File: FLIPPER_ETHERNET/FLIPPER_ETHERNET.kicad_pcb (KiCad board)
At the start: 2 copper layers, 31 parts, among them IC1 MC74ACT125DTR2G, J1 RJ45_Hanrun_HR911105A_Horizon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, J2 Screw_Terminal_01x06, SW1 SW_Push, T1 HX1188NLT, U1 ENC28J60x-ML, Y1 25MHz

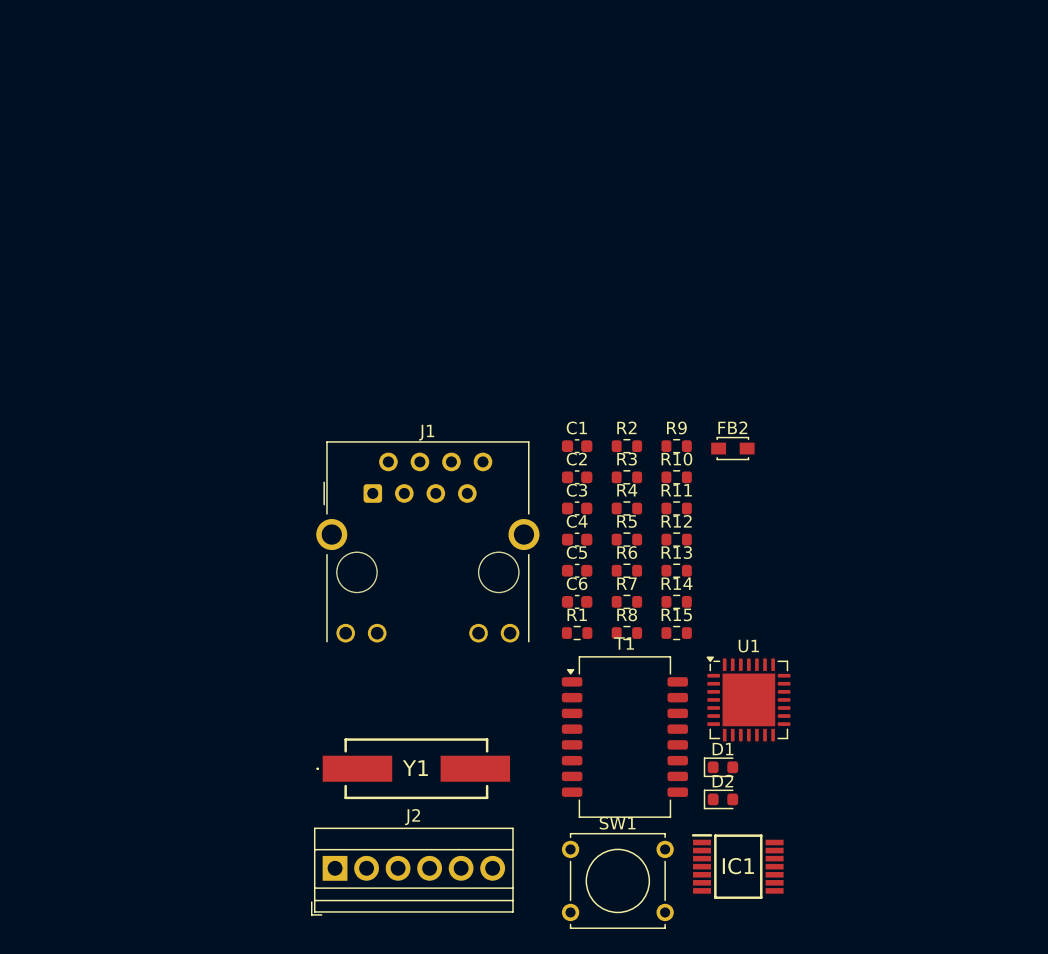
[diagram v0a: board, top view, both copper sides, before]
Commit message: feat: component reduction in the schematic of flipper ethernet and pcb first draft
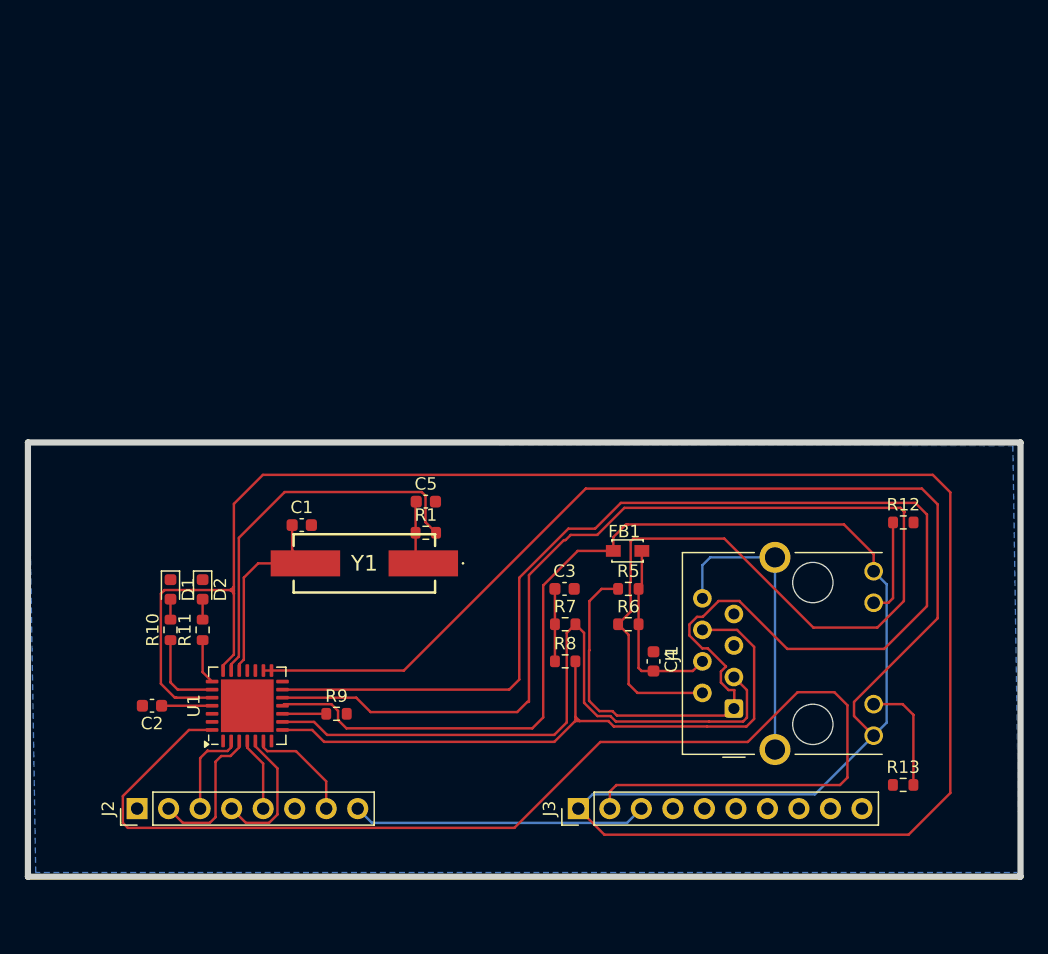
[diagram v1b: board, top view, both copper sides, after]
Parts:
- removed C6: 18pF, Capacitor_SMD:C_0603_1608Metric
- removed FB2: ILBB0805ER202V, Inductor_SMD:L_Walsin_WLFM201209x
- removed IC1: MC74ACT125DTR2G, FLIPPER_ETHERNET:MC74ACT125DTR2G
- removed R14: 100R, Resistor_SMD:R_0603_1608Metric
- removed R15: 10K, Resistor_SMD:R_0603_1608Metric
- removed R2, R3, R4: 75R, Resistor_SMD:R_0603_1608Metric
- removed SW1: SW_Push, Button_Switch_THT:SW_Tactile_Straight_KSA0Axx1LFTR
- removed T1: HX1188NLT, Transformer_SMD:Transformer_Pulse_H1100NL
- added FB1: FerriteBead, Inductor_SMD:L_Walsin_WLFM201209x, F.Cu at (159.3, 87.4)
- added J3: Conn_01x10_Socket, Connector_PinHeader_2.54mm:PinHeader_1x10_P2.54mm_Vertical, F.Cu at (155.3, 108.2)
- C1: value 1nF -> 18pF
- J2: value Screw_Terminal_01x06 -> Conn_01x08_Socket; footprint TerminalBlock:TerminalBlock_Xinya_XY308-2.54-6P_1x06_P2.54mm_Horizontal -> Connector_PinHeader_2.54mm:PinHeader_1x08_P2.54mm_Vertical
- R1: value 75R -> 100R
- moved D1 46.8 mm to (122.5, 90.5), turned to -90 degrees
- moved D2 45.2 mm to (125.0, 90.5), turned to -90 degrees
- moved R10 42.6 mm to (122.5, 93.8), turned to 90 degrees
- moved U1 40.4 mm to (128.6, 99.9), turned to 90 degrees
- moved R11 39.4 mm to (125.0, 93.8), turned to 90 degrees
- moved C2 38.9 mm to (121.0, 99.9), turned to 180 degrees
- moved R9 34.9 mm to (135.8, 100.5)
- moved J1 33.9 mm to (167.9, 100.1), turned to 90 degrees
- moved R13 25.1 mm to (181.5, 106.2), turned to 180 degrees
- moved C1 23.1 mm to (133.0, 85.3)
- moved R12 18.3 mm to (181.5, 85.1)
- moved Y1 17.1 mm to (138.1, 88.4), turned to 180 degrees
- moved J2 16.7 mm to (119.8, 108.2), turned to 90 degrees
- moved R1 14.6 mm to (143.0, 85.9)
- moved C5 13.4 mm to (143.0, 83.4)
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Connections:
- net Net-(U1-LEDA) renamed /LEDA
- net Net-(U1-LEDB) renamed /LEDB
- C1 pad 1: Net-(C1-Pad1) -> /OSC1
- C5 pad 1: /OSC1 -> Net-(C5-Pad1)
- J1 pad 1: /TX+ -> /TD+
- J1 pad 2: /TX- -> /TD-
- J1 pad 3: /RX+ -> /RD+
- J1 pad 4: Net-(J1-RCT) -> /TCT
- J1 pad 5: Net-(J1-RCT) -> unconnected-(J1-RCT-Pad5)
- J1 pad 6: /RX- -> /RD-
- J1 pad 8: Net-(J1-Pad8) -> GND
- J2 pad 1: /CS -> unconnected-(J2-Pin_1-Pad1)
- J2 pad 2: /MSCK -> /SI
- J2 pad 3: /MSO -> /SO
- J2 pad 4: /MSI -> /CS
- J2 pad 5: /MOSC1 -> /SCK
- J2 pad 6: /MINT0 -> unconnected-(J2-Pin_6-Pad6)
- R1 pad 1: /CMT_R -> Net-(C5-Pad1)
- R1 pad 2: Net-(C1-Pad1) -> /OSC2
- R5 pad 1: /TPOUT+ -> /TD+
- R6 pad 2: /TPOUT- -> /TD-
- R7 pad 1: /TPIN+ -> /RD+
- R8 pad 2: /TPIN- -> /RD-
- U1 pad 12: /TPOUT- -> /TD-
- U1 pad 13: /TPOUT+ -> /TD+
- U1 pad 27: /CLKOUT -> unconnected-(U1-CLKOUT-Pad27)
- U1 pad 3: /MSO -> /SI
- U1 pad 4: /MSCK -> /SCK
- U1 pad 6: /RESET -> /RST
- U1 pad 8: /TPIN- -> /RD-
- U1 pad 9: /TPIN+ -> /RD+
- Y1 pad 1: Net-(C6-Pad1) -> Net-(C5-Pad1)
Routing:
- net +3.3V: track 0.00 -> 336.7 mm
- net /TD+: track 0.00 -> 126.0 mm
- net /TD-: track 0.00 -> 115.4 mm
- net /INT: track 0.00 -> 101.9 mm
- net /RD+: track 0.00 -> 56.2 mm
- net /RD-: track 0.00 -> 55.4 mm
- net GND: track 0.00 -> 48.1 mm
- net /OSC2: track 0.00 -> 31.0 mm
- net /OSC1: track 0.00 -> 17.3 mm
- net /TCT: track 0.00 -> 15.1 mm
- net /SI: track 0.00 -> 11.8 mm
- net /CS: track 0.00 -> 11.1 mm
- net Net-(J1-Pad10): track 0.00 -> 9.21 mm
- net /RST: track 0.00 -> 8.91 mm
- net Net-(J1-Pad11): track 0.00 -> 7.82 mm
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- added copper zone on B.Cu, net (none)
- added copper zone on F.Cu, net GND
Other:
- board outline added: 80 x 35 mm

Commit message: feat: second draft of flipper ethernet pcb
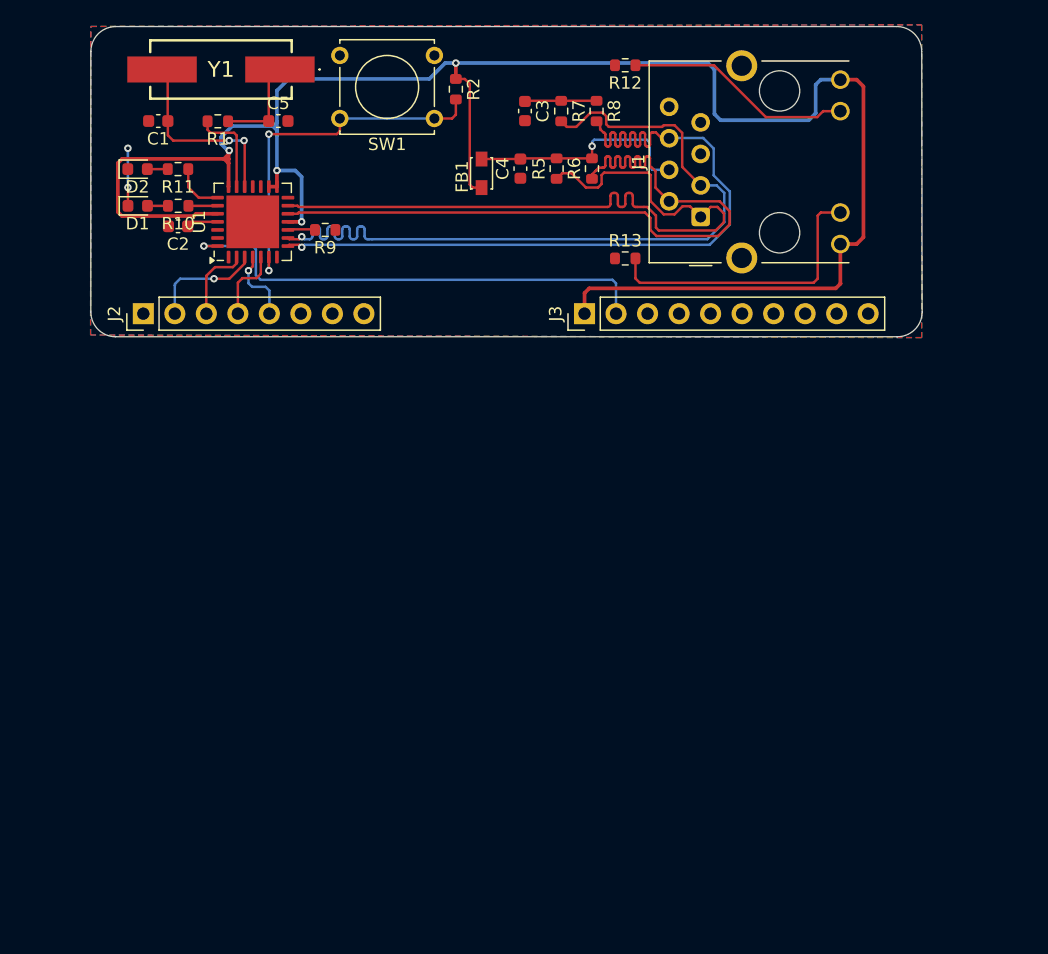
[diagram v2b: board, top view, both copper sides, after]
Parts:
- added R2: 10K, Resistor_SMD:R_0603_1608Metric, F.Cu at (145.4, 50.2)
- added SW1: SW_Push, Button_Switch_THT:SW_Tactile_Straight_KSA0Axx1LFTR, F.Cu at (143.7, 52.5)
- moved R13 48.0 mm to (159.1, 63.8)
- moved R8 44.4 mm to (156.8, 51.9), turned to -90 degrees
- moved R12 43.1 mm to (159.1, 48.2), turned to 180 degrees
- moved Y1 41.4 mm to (126.5, 48.6)
- moved R7 41.4 mm to (153.9, 51.9), turned to 90 degrees
- moved C4 41.1 mm to (150.7, 56.6), turned to -90 degrees
- moved J2 39.9 mm to (120.3, 68.3)
- moved J3 39.9 mm to (155.8, 68.3)
- moved J1 39.7 mm to (165.2, 60.5)
- moved R9 39.0 mm to (134.9, 61.5)
- moved U1 39.0 mm to (129.1, 60.9)
- moved C2 38.7 mm to (123.1, 61.2)
- moved C3 38.6 mm to (151.0, 51.9), turned to -90 degrees
- moved R11 37.2 mm to (123.1, 56.6), turned to 180 degrees
- moved R1 37.2 mm to (126.3, 52.8), turned to 180 degrees
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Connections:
- J2 pad 7: /RST -> unconnected-(J2-Pin_7-Pad7)
- U1 pad 6: /RST -> /RESET
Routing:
- net +3.3V: track 336.7 -> 154.8 mm, vias 0 -> 4
- net /TD+: track 126.0 -> 60.0 mm
- net /INT: track 101.9 -> 39.2 mm, vias 0 -> 1
- net /TD-: track 115.4 -> 60.0 mm
- net GND: track 48.1 -> 4.64 mm, vias 0 -> 2
- net /RESET: track 0.00 -> 29.6 mm, vias 0 -> 2
- net /OSC2: track 31.0 -> 7.34 mm
- net Net-(J1-Pad10): track 9.21 -> 23.6 mm
- net Net-(J1-Pad11): track 7.82 -> 18.5 mm
- net /RST: track 8.91 -> 0.00 mm
- net /RD-: track 55.4 -> 63.5 mm, vias 0 -> 1
- net /RD+: track 56.2 -> 63.4 mm, vias 0 -> 1
- net /CS: track 11.1 -> 6.00 mm
- net /LEDA: track 7.00 -> 2.35 mm
- net /TCT: track 15.1 -> 18.7 mm, vias 0 -> 1
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- added copper zone on B.Cu, net GND
- removed copper zone on B.Cu, net (none)
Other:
- board size 80 x 35 mm -> 67 x 25 mm

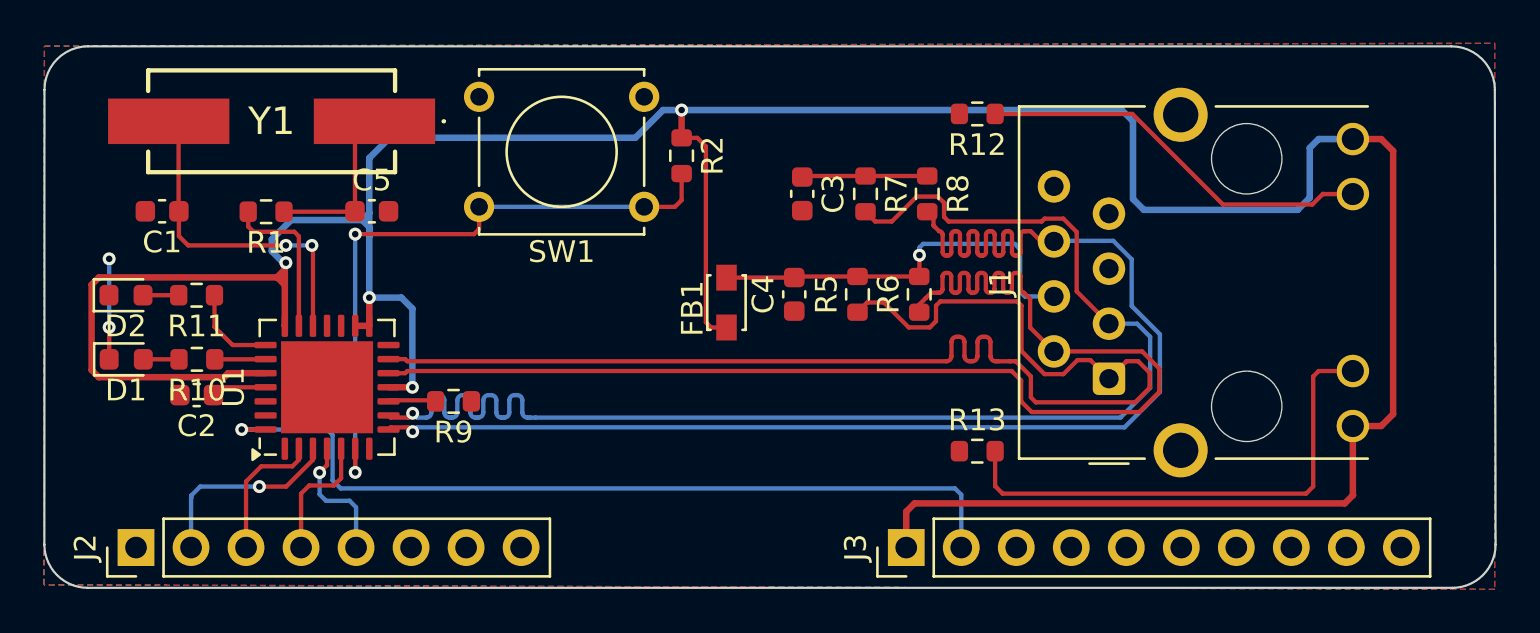
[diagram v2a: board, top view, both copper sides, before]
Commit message: feat: pcb corrected for possible first flipper ethernet prototype
all 3d models added
all labels added and reorganized
button changed for smd metal button
components reorganized
leds deleted
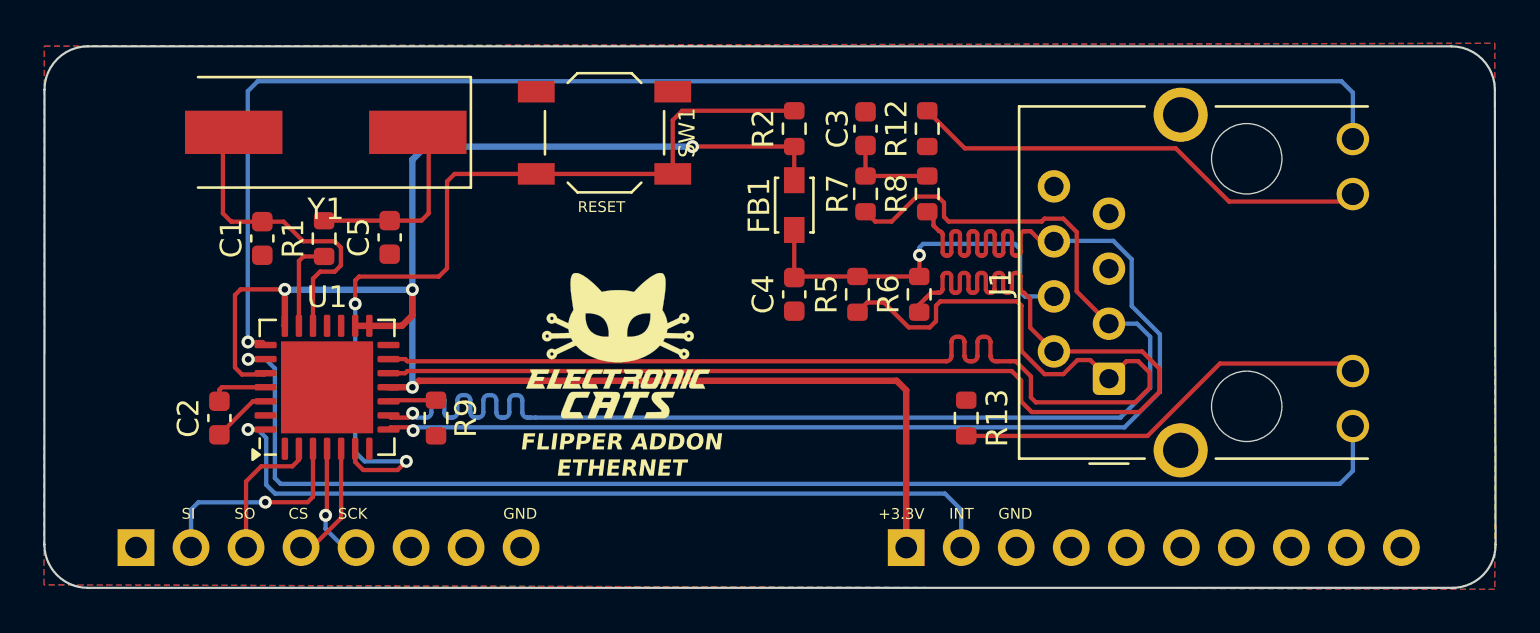
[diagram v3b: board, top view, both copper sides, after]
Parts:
- removed D1, D2: LED, LED_SMD:LED_0603_1608Metric
- removed R10, R11: 30R, Resistor_SMD:R_0603_1608Metric
- added G***: LOGO, Aesthetics:electronic_cats_logo_8x6, F.Cu at (142.5, 59.0)
- added G***: LOGO, Aesthetics:electronic_cats_logo_8x6, B.Cu at (142.5, 59.0)
- added REF**: OSHW-Logo2_9.8x8mm_SilkScreen, Symbol:OSHW-Logo2_9.8x8mm_SilkScreen, B.Cu at (153.7, 60.4)
- J2, J3: moved to B.Cu
- SW1: footprint Button_Switch_THT:SW_Tactile_Straight_KSA0Axx1LFTR -> Button_Switch_SMD:SW_SPST_TL3342
- Y1: footprint FLIPPER_ETHERNET:ABLS-25.000MHZ-20-F-T -> Crystal:Crystal_SMD_HC49-SD
- moved FB1 5.48 mm to (150.7, 52.5), turned to -90 degrees
- moved R2 5.35 mm to (150.7, 48.9), turned to 90 degrees
- moved C1 4.79 mm to (126.1, 54.0), turned to -90 degrees
- moved C3 4.19 mm to (153.9, 48.9), turned to 90 degrees
- moved SW1 3.88 mm to (141.9, 49.1)
- moved R1 2.95 mm to (128.9, 54.0), turned to -90 degrees
- moved Y1 2.55 mm to (129.0, 49.1)
- moved R12 2.41 mm to (156.8, 48.9), turned to -90 degrees
- moved R13 1.61 mm to (158.6, 62.3), turned to 90 degrees
- moved C2 1.49 mm to (124.1, 62.3), turned to -90 degrees
- moved C5 1.46 mm to (132.0, 54.0), turned to -90 degrees
- moved R9 1.12 mm to (134.1, 62.3), turned to -90 degrees
- turned J2 to -90 degrees
- turned J3 to -90 degrees
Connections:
- J1 pad 12: +3.3V -> /LEDB
- J1 pad 9: +3.3V -> /LEDA
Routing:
- net +3.3V: track 154.8 -> 80.4 mm
- net /LEDB: track 4.17 -> 66.0 mm, vias 0 -> 1
- net /LEDA: track 2.35 -> 59.5 mm, vias 0 -> 1
- net /RESET: track 29.6 -> 41.1 mm
- net Net-(J1-Pad10): track 23.6 -> 19.4 mm
- net /OSC2: track 7.34 -> 4.24 mm
- net Net-(J1-Pad11): track 18.5 -> 21.5 mm
- net GND: track 4.64 -> 2.77 mm, vias 2 -> 0
- net Net-(D2-A): track 1.65 -> 0.00 mm
- net Net-(D1-A): track 1.65 -> 0.00 mm
- net Net-(C3-Pad1): track 5.80 -> 4.27 mm
- net /INT: track 39.2 -> 38.3 mm
- net /TCT: track 18.7 -> 17.8 mm
- net Net-(C5-Pad1): track 7.82 -> 8.71 mm
- net /OSC1: track 15.9 -> 15.0 mm, vias 2 -> 0
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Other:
- board text added: "+3.3V"
- board text added: "CS"
- board text added: "FLIPPER ADDON ETHERNET"
- board text added: "GND"
- board text added: "INT"
- board text added: "RESET"
- board text added: "SCK"
- board text added: "SI"
- board text added: "SO"

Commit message: feat: add labels
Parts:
- added kibuzzard-6706978D: G***, kibuzzard-6706978D, F.Cu at (142.0, 53.4)
- added kibuzzard-670697AB: G***, kibuzzard-670697AB, F.Cu at (130.8, 66.0)
- added kibuzzard-670697C4: G***, kibuzzard-670697C4, F.Cu at (127.7, 65.8)
- added kibuzzard-670697CE: G***, kibuzzard-670697CE, F.Cu at (125.2, 65.7)
- added kibuzzard-670697DC: G***, kibuzzard-670697DC, F.Cu at (122.8, 65.9)
- added kibuzzard-6706980D: G***, kibuzzard-6706980D, F.Cu at (137.7, 66.0)
- added kibuzzard-6706982B: G***, kibuzzard-6706982B, F.Cu at (161.4, 66.2)
- added kibuzzard-67069833: G***, kibuzzard-67069833, F.Cu at (158.3, 65.5)
- added kibuzzard-67069840: G***, kibuzzard-67069840, F.Cu at (155.8, 65.2)
- moved G*** 13.6 mm to (131.9, 50.6)
- moved REF** 9.11 mm to (152.5, 51.4)
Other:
- board text added: "FLIPPER ADDON ETHERNET v1.0"
- board text removed: "+3.3V"
- board text removed: "CS"
- board text removed: "FLIPPER ADDON ETHERNET"
- board text removed: "GND"
- board text removed: "INT"
- board text removed: "RESET"
- board text removed: "SCK"
- board text removed: "SI"
- board text removed: "SO"
